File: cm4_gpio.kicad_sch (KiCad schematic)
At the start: 36 parts, among them CN3 Harwin M20-9990246, U3 SN74LVC1G125DBV

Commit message: getting there
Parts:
- R25: now not fitted
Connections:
- net 3V3_PCIE_EN: now also R24.2; no longer R21.2
- net COMMS_RED: now also CN4.38 (GPIO11); no longer R12.2
- net GNSS_RESET: now also R20.2; no longer R22.2
- net PLL_CLK_SEL: now also R21.2; no longer R24.2
- net PLL_OE: now also R22.2; no longer R18.2
- net PWR_CRITICAL: now also CN4.50 (GPIO17); no longer CN4.47 (GPIO23)
- net REF_CLK_SEL: now also R18.2; no longer R23.2
- net SFP_TX_DISABLE: now also R23.2; no longer R20.2
- net UART3_TX: now also R12.2; no longer CN4.54 (GPIO4)
- net at R12.1: now also CN4.54 (GPIO4); no longer CN4.38 (GPIO11)
- net at R19.1: now also CN4.47 (GPIO23); no longer CN4.50 (GPIO17)
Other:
- moved on the sheet: R19
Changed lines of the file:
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@@
-    (stroke (width 0) (type default))
-  )
-  (wire (pts (xy 179.07 78.74) (xy 187.96 78.74))
     (stroke (width 0) (type default))
   )
@@
     (stroke (width 0) (type default))
   )
-  (wire (pts (xy 218.44 76.2) (xy 251.46 76.2))
+  (wire (pts (xy 218.44 60.96) (xy 251.46 60.96))
     (stroke (width 0) (type default))
   )
@@
     (stroke (width 0) (type default))
   )
-  (wire (pts (xy 227.33 60.96) (xy 218.44 60.96))
+  (wire (pts (xy 227.33 76.2) (xy 218.44 76.2))
     (stroke (width 0) (type default))
   )
@@
     (stroke (width 0) (type default))
   )
-  (wire (pts (xy 134.62 78.74) (xy 171.45 78.74))
-    (stroke (width 0) (type default))
-  )
   (wire (pts (xy 242.57 209.55) (xy 242.57 212.09))
     (stroke (width 0) (type default))
@@
     (stroke (width 0) (type default))
   )
-  (wire (pts (xy 234.95 60.96) (xy 251.46 60.96))
+  (wire (pts (xy 234.95 76.2) (xy 251.46 76.2))
     (stroke (width 0) (type default))
   )
@@
     (stroke (width 0) (type default))
   )
+  (wire (pts (xy 134.62 78.74) (xy 187.96 78.74))
+    (stroke (width 0) (type default))
+  )
   (wire (pts (xy 223.52 138.43) (xy 234.95 138.43))
     (stroke (width 0) (type default))
@@
     (stroke (width 0) (type default))
   )
+  (wire (pts (xy 151.13 60.96) (xy 187.96 60.96))
+    (stroke (width 0) (type default))
+  )
   (wire (pts (xy 189.23 237.49) (xy 189.23 240.03))
     (stroke (width 0) (type default))
@@
     (stroke (width 0) (type default))
   )
-  (wire (pts (xy 134.62 60.96) (xy 187.96 60.96))
+  (wire (pts (xy 134.62 60.96) (xy 143.51 60.96))
     (stroke (width 0) (type default))
   )
@@
     (effects (font (size 1.27 1.27)) (justify right))
   )
-  (hierarchical_label "PWR_CRITICAL" (shape input) (at 251.46 76.2 0) (fields_autoplaced)
+  (hierarchical_label "PWR_CRITICAL" (shape input) (at 251.46 60.96 0) (fields_autoplaced)
     (effects (font (size 1.27 1.27)) (justify left))
   )
@@
     (effects (font (size 1.27 1.27)) (justify right))
   )
-  (hierarchical_label "SFP_TX_DISABLE" (shape output) (at 251.46 66.04 0) (fields_autoplaced)
+  (hierarchical_label "SFP_TX_DISABLE" (shape output) (at 251.46 83.82 0) (fields_autoplaced)
     (effects (font (size 1.27 1.27)) (justify left))
   )
@@
     (effects (font (size 1.27 1.27)) (justify right))
   )
-  (hierarchical_label "REF_CLK_SEL" (shape output) (at 251.46 83.82 0) (fields_autoplaced)
+  (hierarchical_label "REF_CLK_SEL" (shape output) (at 251.46 58.42 0) (fields_autoplaced)
     (effects (font (size 1.27 1.27)) (justify left))
   )
@@
     (effects (font (size 1.27 1.27)) (justify left))
   )
-  (hierarchical_label "RS485_~{RX}{slash}TX" (shape output) (at 251.46 60.96 0) (fields_autoplaced)
+  (hierarchical_label "RS485_~{RX}{slash}TX" (shape output) (at 251.46 76.2 0) (fields_autoplaced)
     (effects (font (size 1.27 1.27)) (justify left))
   )
@@
     (effects (font (size 1.27 1.27)) (justify left))
   )
-  (hierarchical_label "GNSS_RESET" (shape output) (at 251.46 81.28 0) (fields_autoplaced)
+  (hierarchical_label "GNSS_RESET" (shape output) (at 251.46 66.04 0) (fields_autoplaced)
     (effects (font (size 1.27 1.27)) (justify left))
   )
-  (hierarchical_label "PLL_OE" (shape output) (at 251.46 58.42 0) (fields_autoplaced)
+  (hierarchical_label "PLL_OE" (shape output) (at 251.46 81.28 0) (fields_autoplaced)
     (effects (font (size 1.27 1.27)) (justify left))
   )
@@
     (effects (font (size 1.27 1.27)) (justify right))
   )
-  (hierarchical_label "PLL_CLK_SEL" (shape output) (at 251.46 86.36 0) (fields_autoplaced)
+  (hierarchical_label "PLL_CLK_SEL" (shape output) (at 251.46 73.66 0) (fields_autoplaced)
     (effects (font (size 1.27 1.27)) (justify left))
   )
-  (hierarchical_label "3V3_PCIE_EN" (shape output) (at 251.46 73.66 0) (fields_autoplaced)
+  (hierarchical_label "3V3_PCIE_EN" (shape output) (at 251.46 86.36 0) (fields_autoplaced)
     (effects (font (size 1.27 1.27)) (justify left))
   )
@@
     )
   )
-  (symbol (lib_id "AAA_Preferred_WUT:KOA Speer RK73H1ETTP33R0F") (at 175.26 78.74 270) (mirror x) (unit 1)
-    (in_bom yes) (on_board yes) (dnp no)
-    (property "Reference" "R12" (at 168.91 77.47 90)
-      (effects (font (size 1.27 1.27)))
-    )
-    (property "Value" "33R" (at 180.975 77.47 90)
-      (effects (font (size 1.27 1.27)))
-    )
-    (property "Footprint" "Resistor_SMD:R_0402_1005Metric" (at 175.26 80.518 90)
-      (effects (font (size 1.27 1.27)) hide)
-    )
-    (property "Datasheet" "https://www.koaspeer.com/pdfs/RK73H.pdf" (at 175.26 78.74 0)
-      (effects (font (size 1.27 1.27)) hide)
-    )
-    (property "MPN" "RK73H1ETTP33R0F" (at 175.26 78.74 0)
-      (effects (font (size 1.27 1.27)) hide)
-    )
-    (property "Manufacturer" "KOA Speer" (at 175.26 78.74 0)
-      (effects (font (size 1.27 1.27)) hide)
-    )
-    (property "Tolerance" "1%" (at 175.26 78.74 0)
-      (effects (font (size 1.27 1.27)) hide)
-    )
-    (property "Height" "0.4mm" (at 175.26 78.74 0)
-      (effects (font (size 1.27 1.27)) hide)
-    )
-    (pin "1")
-    (pin "2")
-    (instances
-      (project "Master Timing Card"
-        (path "/6e8e281e-e30f-459d-852f-231836068db5/3fdc825c-420f-4918-ada8-75992123f8b4"
-          (reference "R12") (unit 1)
-        )
-      )
-    )
-  )
   (symbol (lib_id "Auto_Library_WUT:Kemet C0402C105K4PACTU") (at 279.4 231.14 0) (unit 1)
     (in_bom yes) (on_board yes) (dnp no) (fields_autoplaced)
@@
     )
   )
-  (symbol (lib_id "AAA_Preferred_WUT:KOA Speer RK73H1ETTP1000F") (at 231.14 60.96 90) (unit 1)
+  (symbol (lib_id "AAA_Preferred_WUT:KOA Speer RK73H1ETTP1000F") (at 231.14 76.2 90) (unit 1)
     (in_bom yes) (on_board yes) (dnp no)
-    (property "Reference" "R19" (at 224.79 59.69 90)
-      (effects (font (size 1.27 1.27)))
-    )
-    (property "Value" "100R" (at 237.49 59.69 90)
-      (effects (font (size 1.27 1.27)))
-    )
-    (property "Footprint" "Resistor_SMD:R_0402_1005Metric" (at 231.14 62.738 90)
-      (effects (font (size 1.27 1.27)) hide)
-    )
-    (property "Datasheet" "https://www.koaspeer.com/pdfs/RK73H.pdf" (at 231.14 60.96 0)
-      (effects (font (size 1.27 1.27)) hide)
-    )
-    (property "MPN" "RK73H1ETTP1000F" (at 231.14 60.96 0)
-      (effects (font (size 1.27 1.27)) hide)
-    )
-    (property "Manufacturer" "KOA Speer" (at 231.14 60.96 0)
-      (effects (font (size 1.27 1.27)) hide)
-    )
-    (property "Tolerance" "1%" (at 231.14 60.96 0)
-      (effects (font (size 1.27 1.27)) hide)
-    )
-    (property "Height" "0.4mm" (at 231.14 60.96 0)
+    (property "Reference" "R19" (at 224.79 74.93 90)
+      (effects (font (size 1.27 1.27)))
+    )
+    (property "Value" "100R" (at 237.49 74.93 90)
+      (effects (font (size 1.27 1.27)))
+    )
+    (property "Footprint" "Resistor_SMD:R_0402_1005Metric" (at 231.14 77.978 90)
+      (effects (font (size 1.27 1.27)) hide)
+    )
+    (property "Datasheet" "https://www.koaspeer.com/pdfs/RK73H.pdf" (at 231.14 76.2 0)
+      (effects (font (size 1.27 1.27)) hide)
+    )
+    (property "MPN" "RK73H1ETTP1000F" (at 231.14 76.2 0)
+      (effects (font (size 1.27 1.27)) hide)
+    )
+    (property "Manufacturer" "KOA Speer" (at 231.14 76.2 0)
+      (effects (font (size 1.27 1.27)) hide)
+    )
+    (property "Tolerance" "1%" (at 231.14 76.2 0)
+      (effects (font (size 1.27 1.27)) hide)
+    )
+    (property "Height" "0.4mm" (at 231.14 76.2 0)
       (effects (font (size 1.27 1.27)) hide)
     )
@@
     )
   )
+  (symbol (lib_id "AAA_Preferred_WUT:KOA Speer RK73H1ETTP33R0F") (at 147.32 60.96 270) (mirror x) (unit 1)
+    (in_bom yes) (on_board yes) (dnp no)
+    (property "Reference" "R12" (at 140.97 59.69 90)
+      (effects (font (size 1.27 1.27)))
+    )
+    (property "Value" "33R" (at 153.035 59.69 90)
+      (effects (font (size 1.27 1.27)))
+    )
+    (property "Footprint" "Resistor_SMD:R_0402_1005Metric" (at 147.32 62.738 90)
+      (effects (font (size 1.27 1.27)) hide)
+    )
+    (property "Datasheet" "https://www.koaspeer.com/pdfs/RK73H.pdf" (at 147.32 60.96 0)
+      (effects (font (size 1.27 1.27)) hide)
+    )
+    (property "MPN" "RK73H1ETTP33R0F" (at 147.32 60.96 0)
+      (effects (font (size 1.27 1.27)) hide)
+    )
+    (property "Manufacturer" "KOA Speer" (at 147.32 60.96 0)
+      (effects (font (size 1.27 1.27)) hide)
+    )
+    (property "Tolerance" "1%" (at 147.32 60.96 0)
+      (effects (font (size 1.27 1.27)) hide)
+    )
+    (property "Height" "0.4mm" (at 147.32 60.96 0)
+      (effects (font (size 1.27 1.27)) hide)
+    )
+    (pin "1")
+    (pin "2")
+    (instances
+      (project "Master Timing Card"
+        (path "/6e8e281e-e30f-459d-852f-231836068db5/3fdc825c-420f-4918-ada8-75992123f8b4"
+          (reference "R12") (unit 1)
+        )
+      )
+    )
+  )
   (symbol (lib_id "Auto_Library_WUT:KOA Speer RK73H1ETTP4701F") (at 138.43 49.53 0) (unit 1)
     (in_bom yes) (on_board yes) (dnp no) (fields_autoplaced)
@@
   )
   (symbol (lib_id "AAA_Preferred_WUT:KOA Speer RK73Z1ETTP") (at 233.68 133.35 90) (unit 1)
-    (in_bom yes) (on_board yes) (dnp no)
+    (in_bom yes) (on_board yes) (dnp yes)
     (property "Reference" "R25" (at 229.87 132.08 90)
       (effects (font (size 1.27 1.27)) (justify left))

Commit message: committing before attempting scripting
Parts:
- renumbered R9 to R10, R10 to R11, R18 to R12, R20 to R18, R21 to R19, R19 to R20, R22 to R21, R23 to R22, R24 to R23, R25 to R24, R11 to R25, R12 to R9
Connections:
- net COMMS_GREEN: now also CN4.28 (GPIO13); no longer CN4.44 (GPIO10)
- net COMMS_RED: now also CN4.40 (GPIO9); no longer CN4.38 (GPIO11)
- net PLL_LOCK: now also CN4.39 (GPIO8); no longer CN4.27 (GPIO20)
- net REF_CLK_SEL: now also R12.1; no longer R12.2
- net SFP_TX_FAULT: now also CN4.27 (GPIO20); no longer CN4.40 (GPIO9)
- net STATUS_GREEN: now also CN4.38 (GPIO11); no longer CN4.31 (GPIO12)
- net STATUS_RED: now also CN4.44 (GPIO10); no longer CN4.28 (GPIO13)
- net ~{SFP_PRESENT}: now also CN4.26 (GPIO19); no longer CN4.39 (GPIO8)
- net at CN4.29 (GPIO16): now also R18.1; no longer R12.1
- new net: CN4.31 (GPIO12), R12.2
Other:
- moved on the sheet: R12, R17, R18, R25, R26

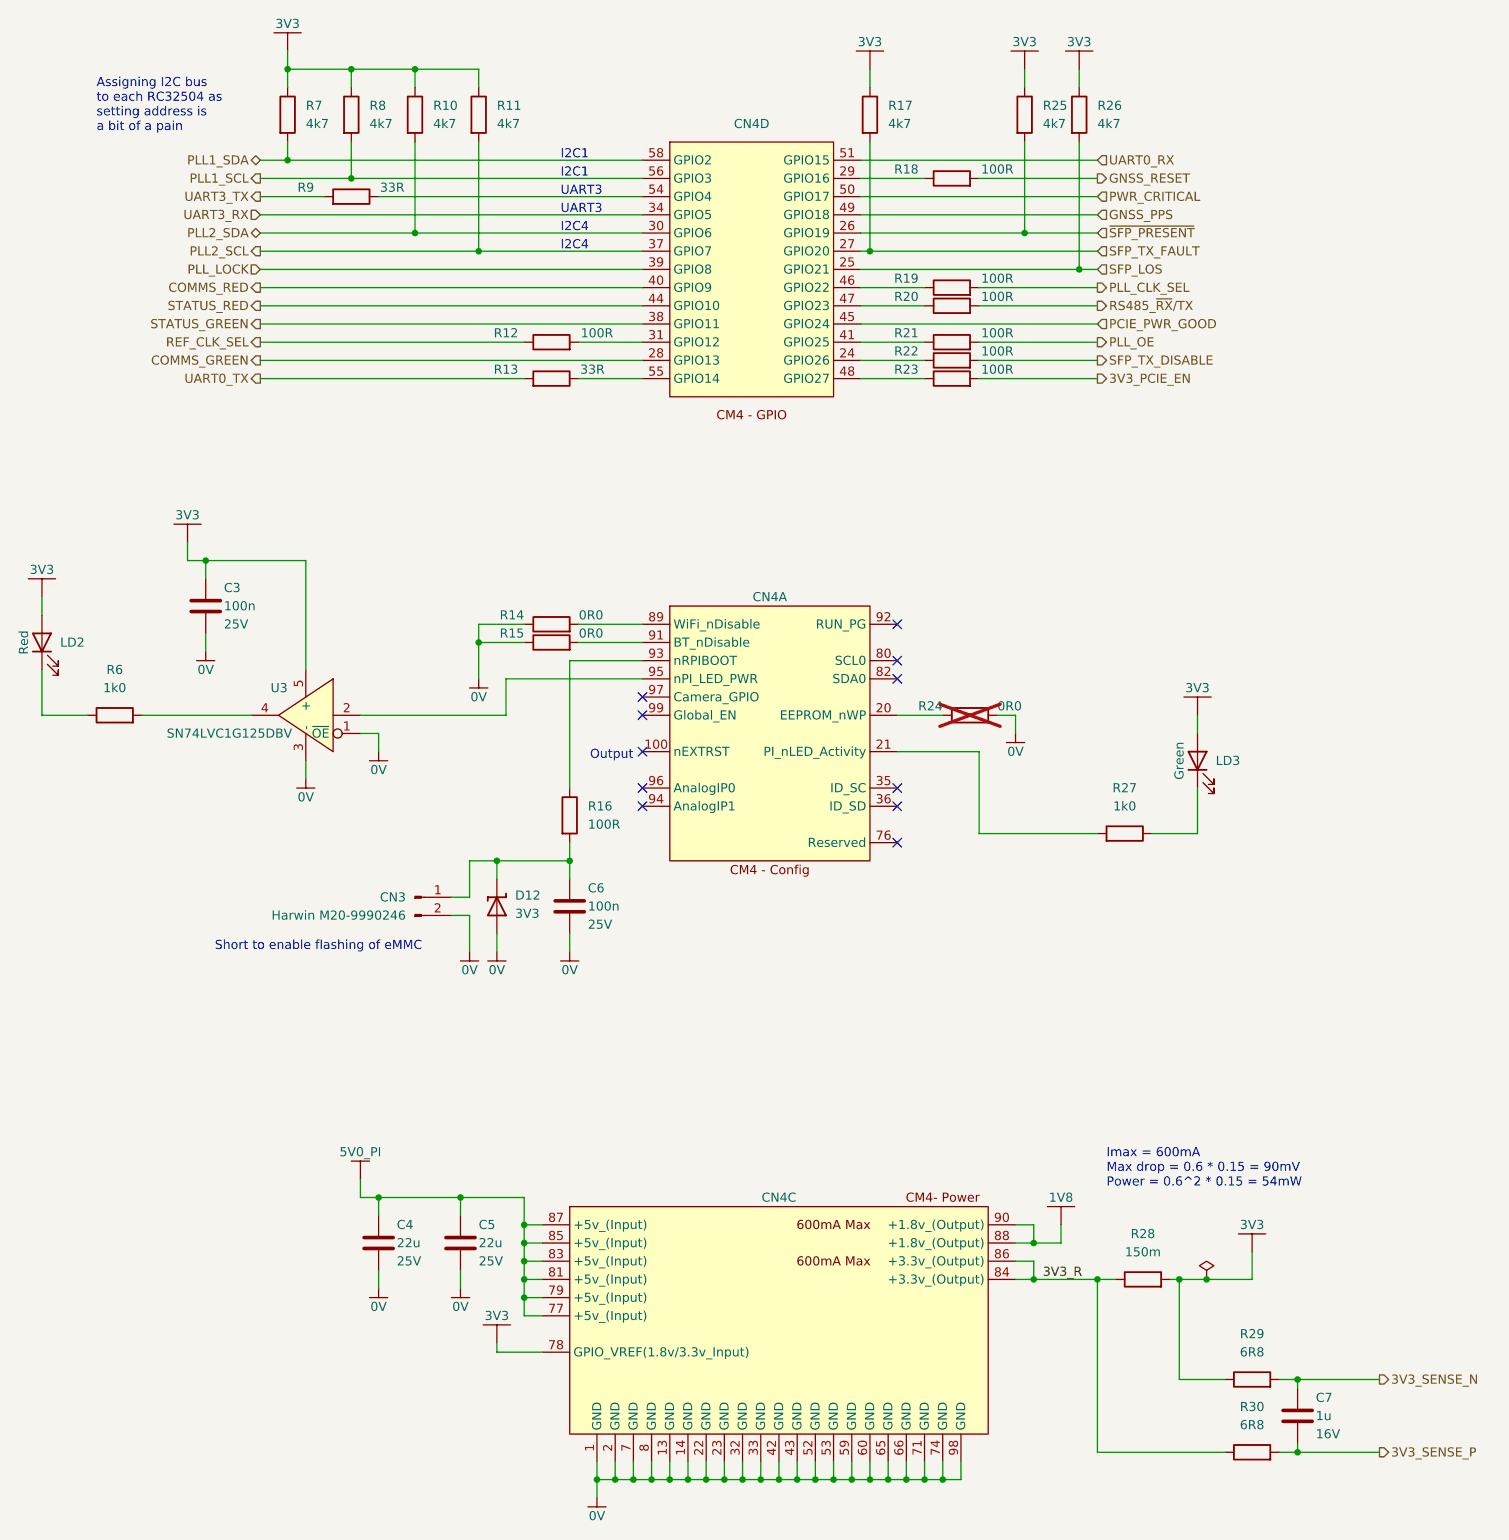
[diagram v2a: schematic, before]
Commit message: Fixed connector offsets
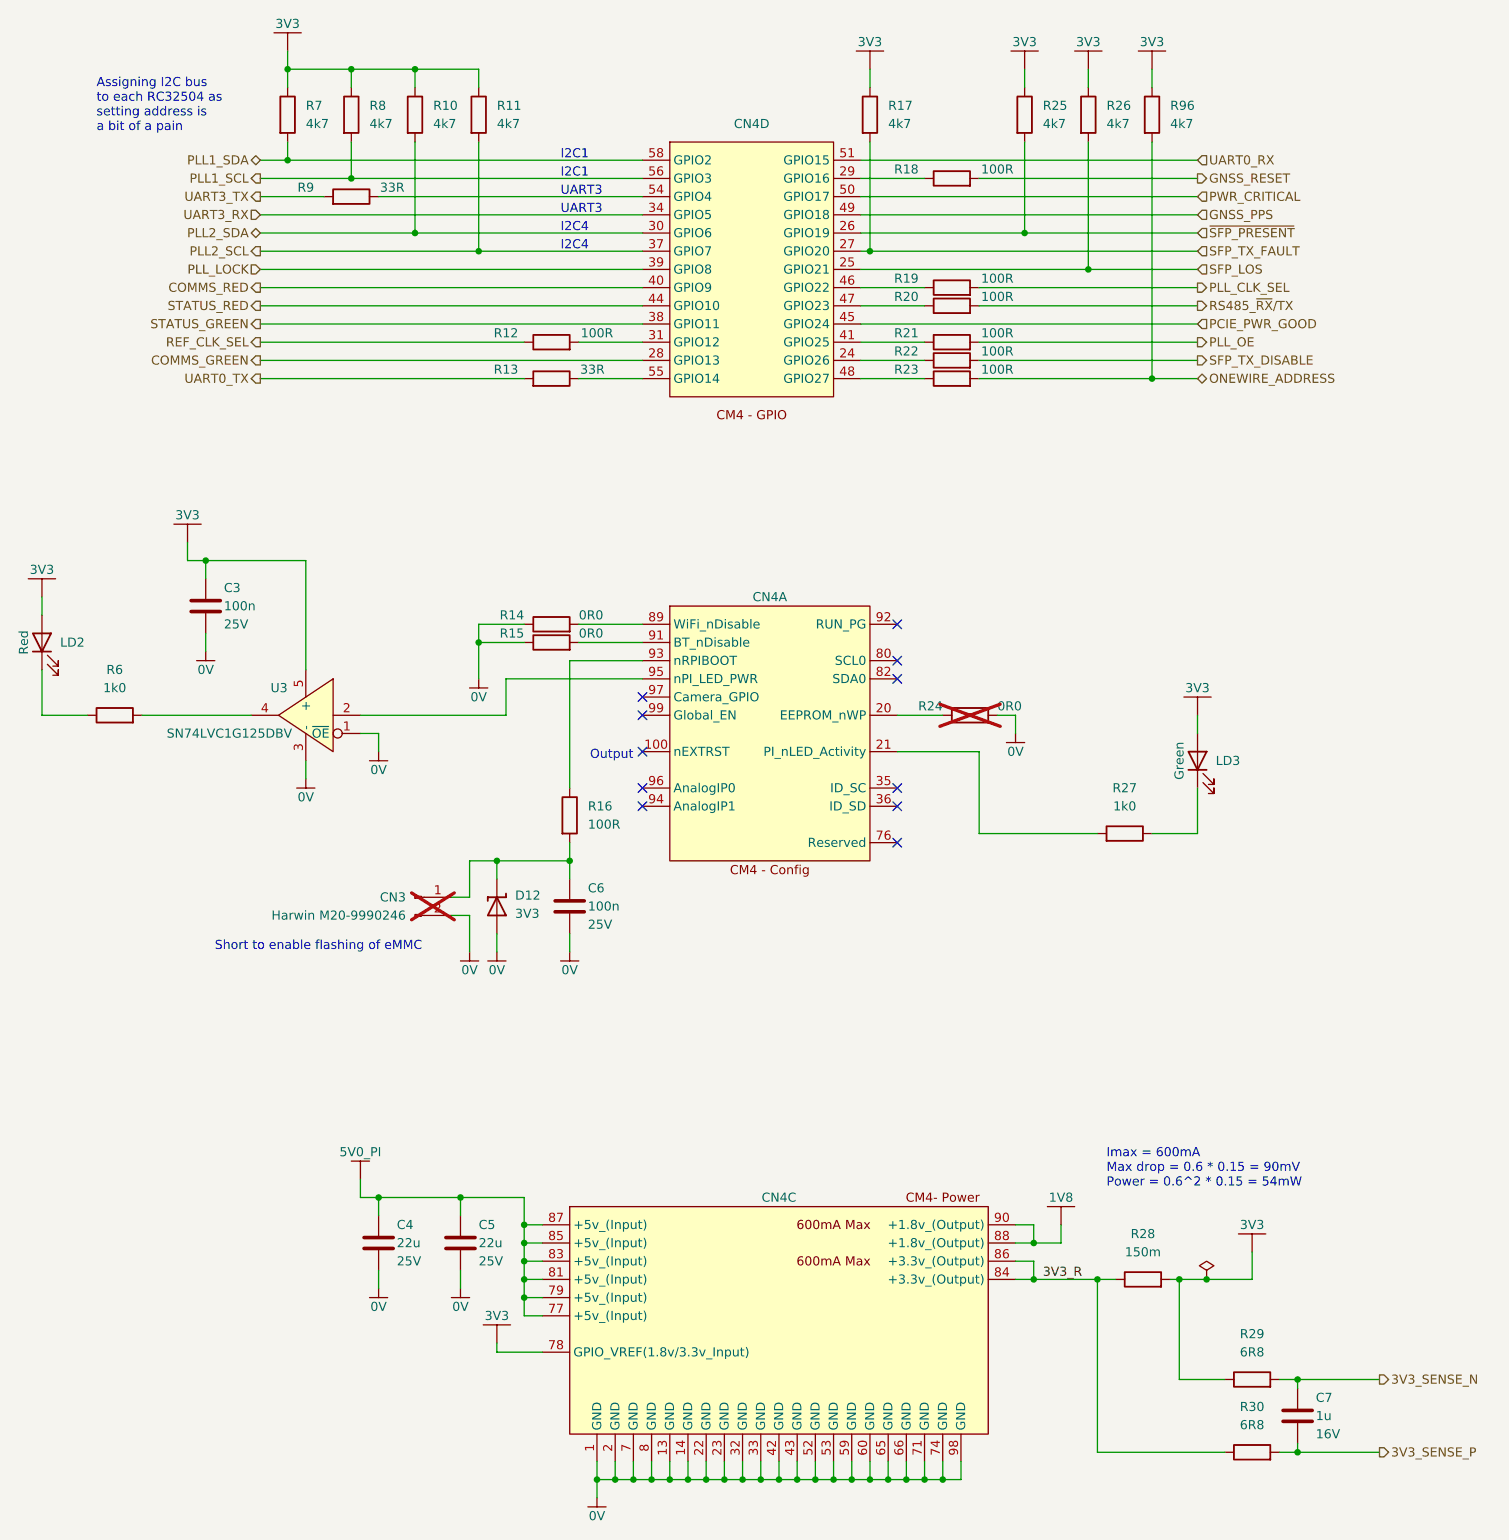
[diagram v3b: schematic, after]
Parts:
- added R96: 4k7, Resistor_SMD:R_0402_1005Metric, symbol Auto_Library_WUT:KOA Speer RK73H1ETTP4701F
- CN3: now not fitted
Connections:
- net 3V3: now also R96.1
- net 3V3_PCIE_EN renamed ONEWIRE_ADDRESS
- net ONEWIRE_ADDRESS: now also R96.2
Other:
- moved on the sheet: R26
